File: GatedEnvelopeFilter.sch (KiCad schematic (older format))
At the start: 36 parts, among them U1 4069UB, U2 4066BMS

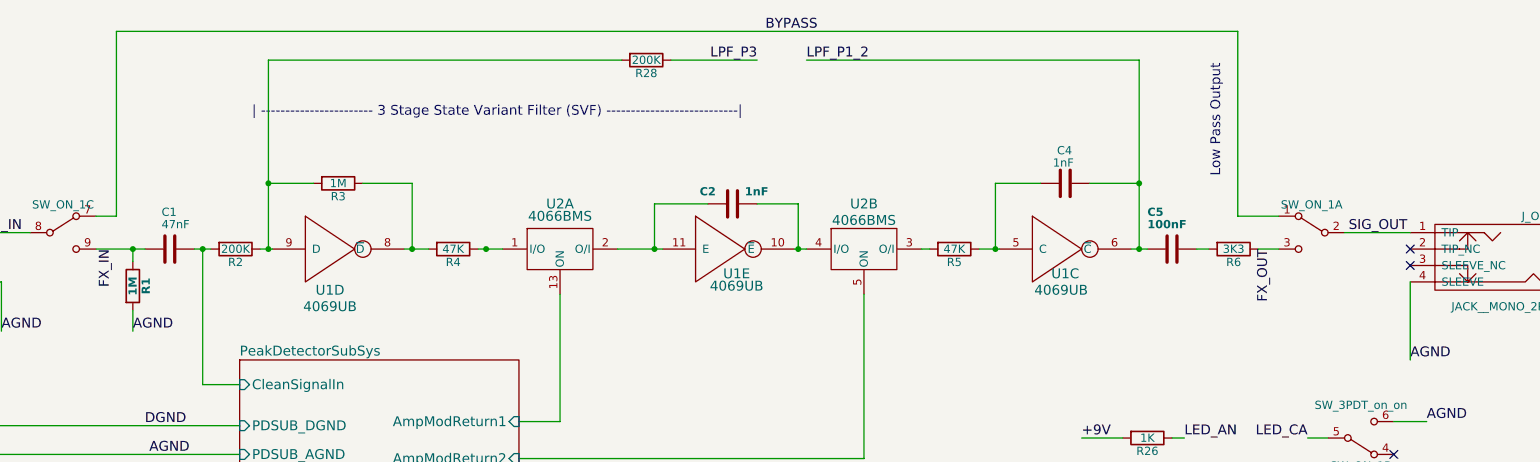
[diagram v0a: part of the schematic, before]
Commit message: Added output level pot control
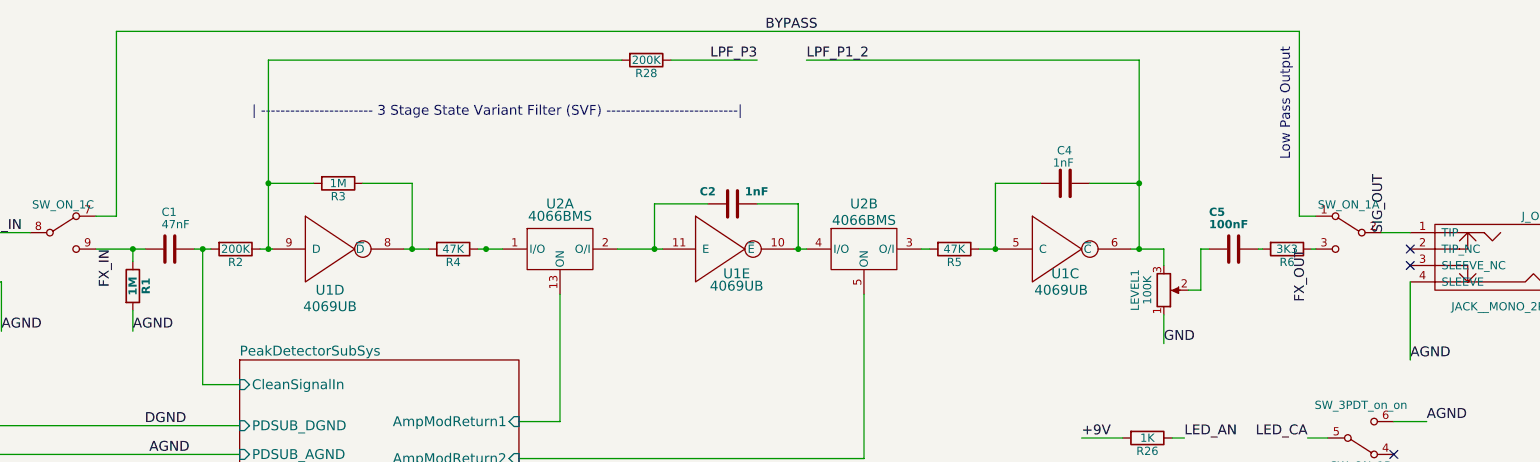
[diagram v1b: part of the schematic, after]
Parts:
- added LEVEL1: 100K, symbol NPOT
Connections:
- net FX_OUT: no longer R6.1, SW_ON_1.3 (C)
- net GND: now also LEVEL1.1
- net LPF_P1_2: now also LEVEL1.3; no longer C5.2
- new net: C5.2, LEVEL1.2
- new net: R6.1, SW_ON_1.3 (C)
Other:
- moved on the sheet: C5, R6, SW_ON_1A
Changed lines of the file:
@@
 L C C5
 U 1 1 5A2AF632
-P 8725 2375
-F 0 "C5" V 8500 2225 50  0000 L CNB
-F 1 "100nF" V 8575 2225 50  0000 L CNB
-F 2 "Capacitors_SMD:C_0805_HandSoldering" H 8763 2225 50  0001 C CNN
-F 3 "" H 8725 2375 50  0001 C CNN
-	1    8725 2375
+P 9100 2375
+F 0 "C5" V 8875 2225 50  0000 L CNB
+F 1 "100nF" V 8950 2225 50  0000 L CNB
+F 2 "Capacitors_SMD:C_0805_HandSoldering" H 9138 2225 50  0001 C CNN
+F 3 "" H 9100 2375 50  0001 C CNN
+	1    9100 2375
 	0    1    1    0
 $EndComp
@@
 L R R6
 U 1 1 5A2AF789
-P 9100 2375
-F 0 "R6" V 9180 2375 50  0000 C CNN
-F 1 "3K3" V 9100 2375 50  0000 C CNN
-F 2 "Resistors_SMD:R_0805_HandSoldering" V 9030 2375 50  0001 C CNN
-F 3 "" H 9100 2375 50  0001 C CNN
-	1    9100 2375
+P 9425 2375
+F 0 "R6" V 9505 2375 50  0000 C CNN
+F 1 "3K3" V 9425 2375 50  0000 C CNN
+F 2 "Resistors_SMD:R_0805_HandSoldering" V 9355 2375 50  0001 C CNN
+F 3 "" H 9425 2375 50  0001 C CNN
+	1    9425 2375
 	0    1    1    0
 $EndComp
@@
 L SW_3PDT_on_on SW_ON_1
 U 1 1 5A2FB6A1
-P 9575 2275
-F 0 "SW_ON_1" H 9575 2445 50  0000 C CNN
-F 1 "SW_3PDT_on_on" H 9575 2075 50  0001 C CNN
-F 2 "custom_sw:SW_3PDT_W18MM_L17.3MM_P5.3MM_D2MM_SolderLugs" H 9575 2275 50  0001 C CNN
-F 3 "" H 9575 2275 50  0001 C CNN
-	1    9575 2275
+P 9800 2275
+F 0 "SW_ON_1" H 9800 2445 50  0000 C CNN
+F 1 "SW_3PDT_on_on" H 9800 2075 50  0001 C CNN
+F 2 "custom_sw:SW_3PDT_W18MM_L17.3MM_P5.3MM_D2MM_SolderLugs" H 9800 2275 50  0001 C CNN
+F 3 "" H 9800 2275 50  0001 C CNN
+	1    9800 2275
 	-1   0    0    -1
 $EndComp
@@
 Text Notes 3125 1575 0    60   ~ 0
 | ----------------------- 3 Stage State Variant Filter (SVF) ---------------------------|
-Text Notes 9025 1250 3    60   ~ 0
+Text Notes 9450 1150 3    60   ~ 0
 Low Pass Output
 $Comp
@@
 Text Label 1725 2275 2    60   ~ 0
 SIG_IN
-Text Label 9800 2275 0    60   ~ 0
+Text Label 10025 2275 1    60   ~ 0
 SIG_OUT
 Text Label 6250 1050 0    60   ~ 0
@@
 Text Label 2275 2375 3    60   ~ 0
 FX_IN
-Text Label 9325 2375 3    60   ~ 0
+Text Label 9550 2375 3    60   ~ 0
 FX_OUT
 NoConn ~ 1950 5950
@@
 	2300 1050 2300 2175
 Wire Wire Line
-	9125 1050 2300 1050
-Wire Wire Line
-	9125 2175 9125 1050
-Wire Wire Line
-	9375 2175 9125 2175
-Wire Wire Line
-	10175 2275 9775 2275
+	9500 1050 2300 1050
+Wire Wire Line
+	9500 2175 9500 1050
+Wire Wire Line
+	9600 2175 9500 2175
+Wire Wire Line
+	10175 2275 10000 2275
 Wire Wire Line
 	2175 2375 2475 2375
@@
 Connection ~ 8525 2375
 Wire Wire Line
-	9250 2375 9375 2375
-Wire Wire Line
-	8875 2375 8950 2375
-Wire Wire Line
-	8475 2375 8575 2375
+	9575 2375 9600 2375
+Wire Wire Line
+	9250 2375 9275 2375
+Wire Wire Line
+	8475 2375 8675 2375
 Wire Wire Line
 	8525 1225 8525 2375
@@
 Wire Wire Line
 	825  3750 900  3750
+$Comp
+L NPOT LEVEL1
+U 1 1 5AB856C1
+P 8675 2625
+F 0 "LEVEL1" V 8500 2625 50  0000 C CNN
+F 1 "100K" V 8575 2625 50  0000 C CNN
+F 2 "" H 8675 2625 50  0001 C CNN
+F 3 "" H 8675 2625 50  0001 C CNN
+	1    8675 2625
+	1    0    0    1
+$EndComp
+Wire Wire Line
+	8675 2375 8675 2475
+Wire Wire Line
+	8825 2625 8900 2625
+Wire Wire Line
+	8900 2625 8900 2375
+Wire Wire Line
+	8900 2375 8950 2375
+Wire Wire Line
+	8675 2775 8675 2950
+Text Label 8675 2950 0    60   ~ 0
+GND
 $EndSCHEMATC
